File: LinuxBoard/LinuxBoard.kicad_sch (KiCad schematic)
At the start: 17 parts

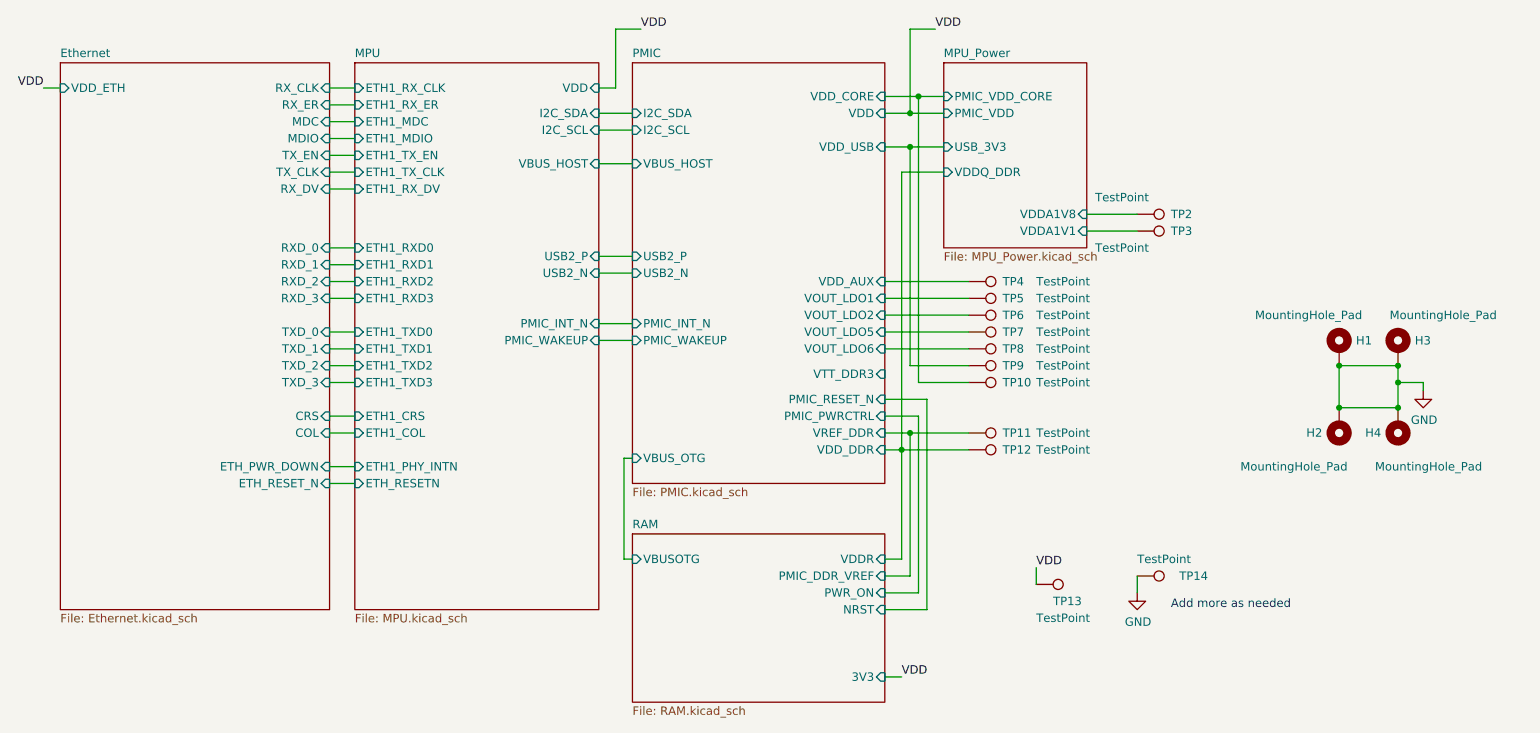
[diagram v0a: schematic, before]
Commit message: Fix ERC errors and reorganize directory
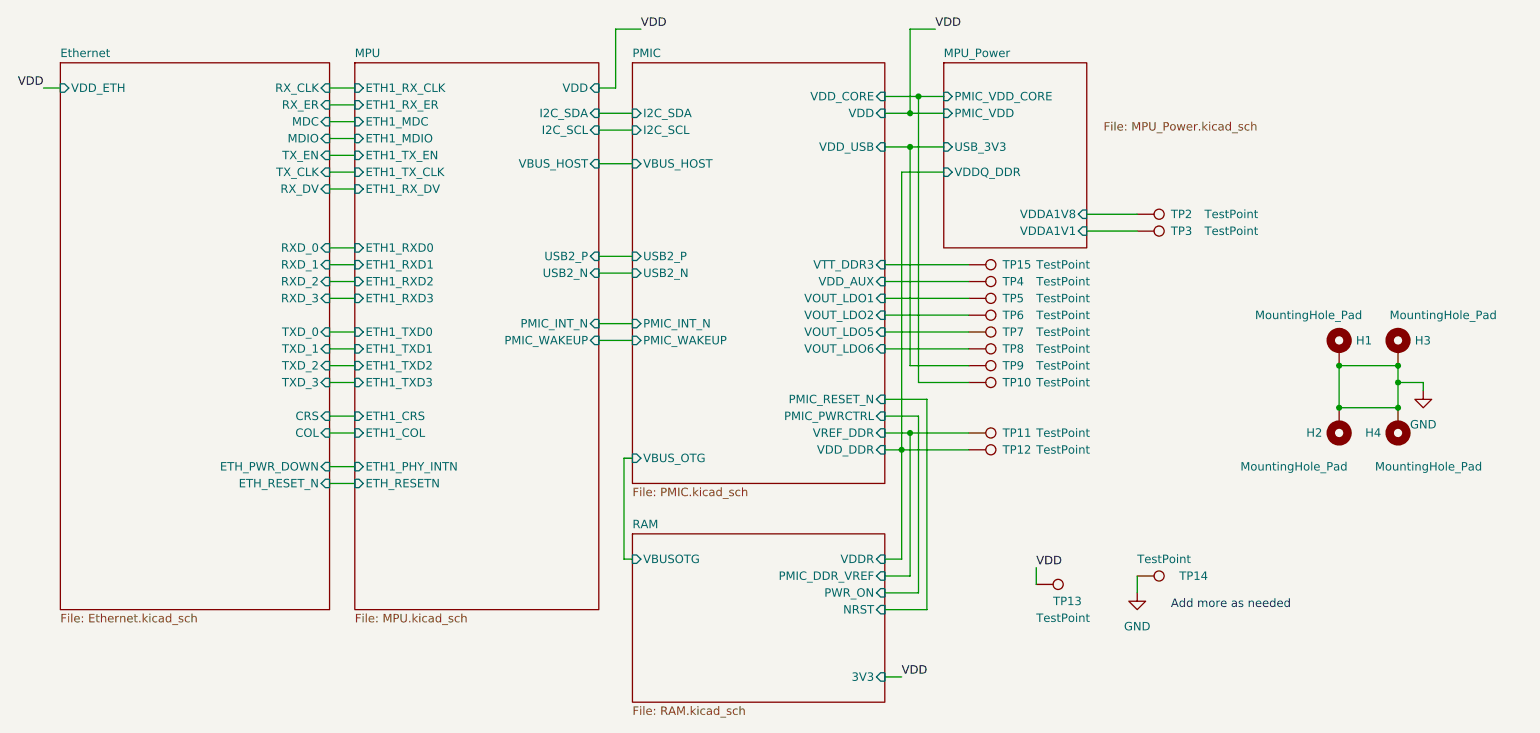
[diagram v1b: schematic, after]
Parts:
- added TP15: TestPoint, TestPoint:TestPoint_Pad_D2.0mm, symbol Connector:TestPoint
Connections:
- net PMIC/VTT_DDR3: now also TP15.1
